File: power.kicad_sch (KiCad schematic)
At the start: 29 parts, among them Q1 DMPH4029LFGQ, Q2 BSS138-7-F, Q3 BSS138-7-F, U1 TPS56C230

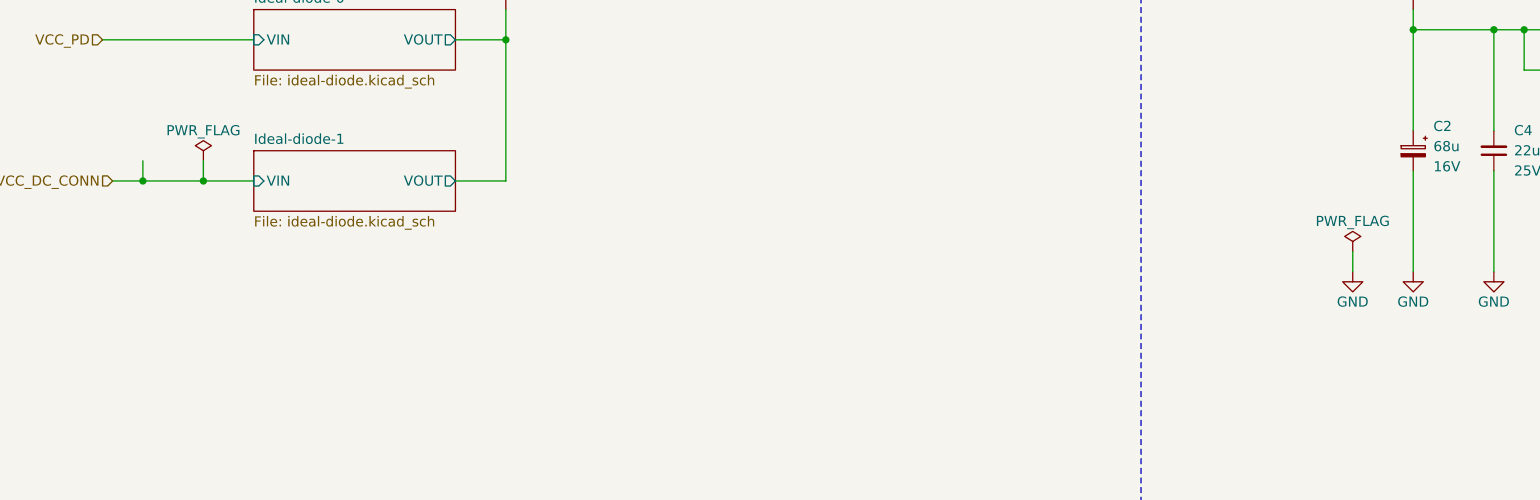
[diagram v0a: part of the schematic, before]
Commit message: [#79262] Add TVS to 12V power pins
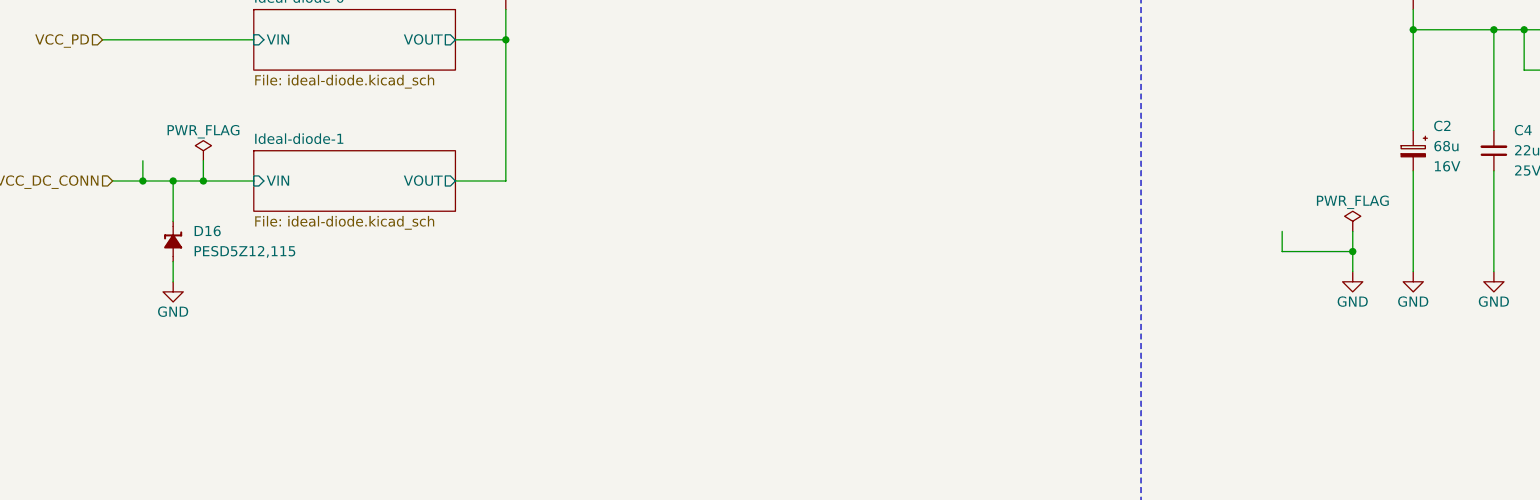
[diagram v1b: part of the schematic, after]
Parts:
- added D16: PESD5Z12, antmicro-footprints:SOD-523, symbol antmicroTVSDiodes:PESD5Z12
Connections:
- net GND: now also D16.2 (A)
- net VCC_DC_CONN: now also D16.1 (C)

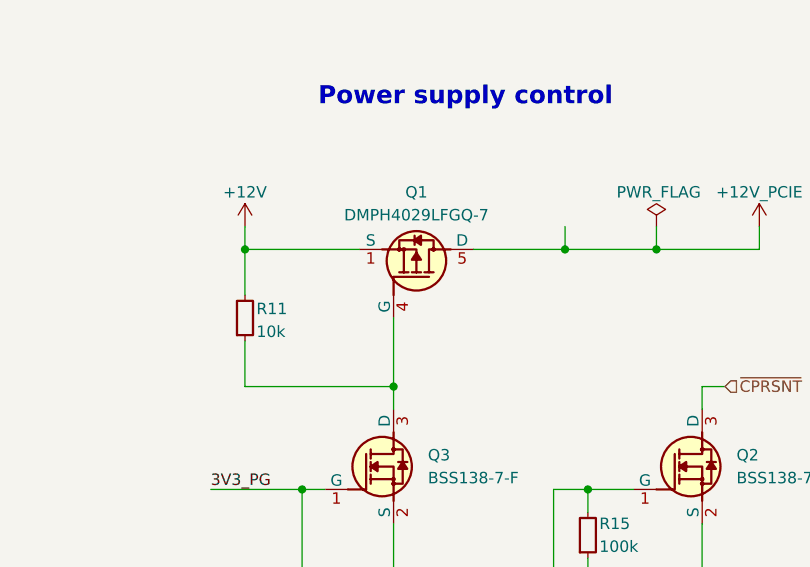
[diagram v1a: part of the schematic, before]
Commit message: [#79262] Further BOM consolidation
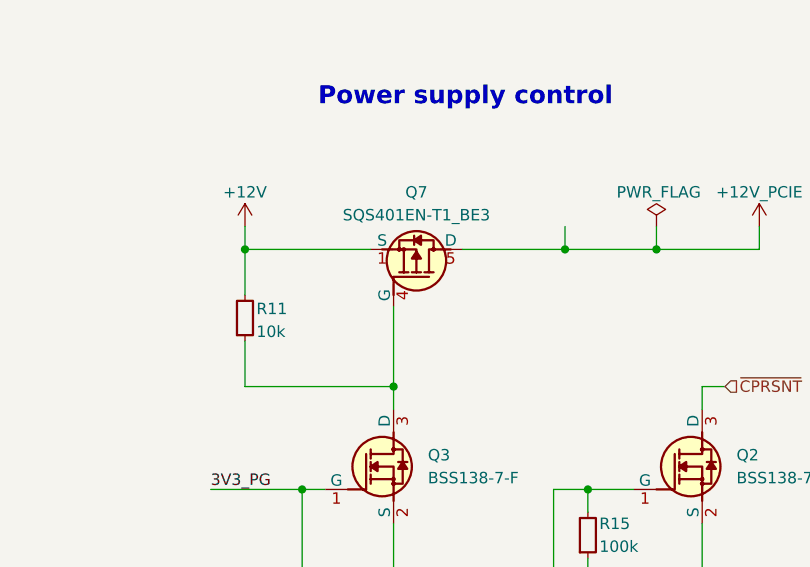
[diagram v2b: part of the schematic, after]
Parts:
- removed Q1: DMPH4029LFGQ, antmicro-footprints:PowerDI3333-8, symbol antmicroTransistorsFETsMOSFETsSingle:DMPH4029LFGQ
- added Q7: SQS401EN-T1_BE3, antmicro-footprints:Vishay_PowerPAK_1212-8_Single, symbol antmicroTransistorsFETsMOSFETsSingle:SQS401EN-T1_BE3
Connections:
- net +12V: now also Q7.1 (S), Q7.2 (S), Q7.3 (S)
- net +12V_PCIE: now also Q7.5 (D)
- net at Q3.3 (D), R11.1: now also Q7.4 (G)
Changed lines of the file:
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@@
 	(wire
 		(pts
-			(xy 99.06 203.2) (xy 99.06 210.82)
-		)
-		(stroke
-			(width 0)
-			(type default)
-		)
-	)
-	(wire
-		(pts
 			(xy 317.5 207.01) (xy 322.58 207.01)
 		)
@@
 	(wire
 		(pts
-			(xy 350.52 77.47) (xy 361.95 77.47)
+			(xy 99.06 201.93) (xy 99.06 210.82)
 		)
 		(stroke
@@
 	(wire
 		(pts
-			(xy 128.27 195.58) (xy 139.7 195.58)
+			(xy 350.52 77.47) (xy 361.95 77.47)
 		)
 		(stroke
@@
 	(wire
 		(pts
-			(xy 107.95 195.58) (xy 118.11 195.58)
+			(xy 128.27 195.58) (xy 139.7 195.58)
 		)
 		(stroke
@@
 	(wire
 		(pts
+			(xy 106.68 195.58) (xy 118.11 195.58)
+		)
+		(stroke
+			(width 0)
+			(type default)
+		)
+	)
+	(wire
+		(pts
 			(xy 361.95 102.87) (xy 361.95 93.98)
 		)
@@
 	(wire
 		(pts
-			(xy 82.55 195.58) (xy 95.25 195.58)
+			(xy 82.55 195.58) (xy 96.52 195.58)
 		)
 		(stroke
@@
 	)
 	(symbol
+		(lib_id "antmicroTransistorsFETsMOSFETsSingle:SQS401EN-T1_BE3")
+		(at 99.06 201.93 270)
+		(mirror x)
+		(unit 1)
+		(exclude_from_sim no)
+		(in_bom yes)
+		(on_board yes)
+		(dnp no)
+		(fields_autoplaced yes)
+		(property "Reference" "Q7"
+			(at 101.6 189.23 90)
+			(effects
+				(font
+					(size 1.27 1.27)
+					(thickness 0.15)
+				)
+			)
+		)
+		(property "Value" "SQS401EN-T1_BE3"
+			(at 88.9 186.69 0)
+			(effects
+				(font
+					(size 1.27 1.27)
+					(thickness 0.15)
+				)
+				(justify left bottom)
+				(hide yes)
+			)
+		)
+		(property "Footprint" "antmicro-footprints:Vishay_PowerPAK_1212-8_Single"
+			(at 86.36 186.69 0)
+			(effects
+				(font
+					(size 1.27 1.27)
+					(thickness 0.15)
+				)
+				(justify left bottom)
+				(hide yes)
+			)
+		)
+		(property "Datasheet" "https://www.vishay.com/docs/65529/sqs401en.pdf"
+			(at 83.82 186.69 0)
+			(effects
+				(font
+					(size 1.27 1.27)
+					(thickness 0.15)
+				)
+				(justify left bottom)
+				(hide yes)
+			)
+		)
+		(property "Description" "MOSFET, P Channel, 40 V, 16A, 0.047 ohm, PowerPAK 1212-8, Surface Mount"
+			(at 99.06 201.93 0)
+			(effects
+				(font
+					(size 1.27 1.27)
+				)
+				(hide yes)
+			)
+		)
+		(property "MPN" "SQS401EN-T1_BE3"
+			(at 101.6 191.77 90)
+			(effects
+				(font
+					(size 1.27 1.27)
+					(thickness 0.15)
+				)
+			)
+		)
+		(property "Manufacturer" "Vishay"
+			(at 81.28 186.69 0)
+			(effects
+				(font
+					(size 1.27 1.27)
+					(thickness 0.15)
+				)
+				(justify left bottom)
+				(hide yes)
+			)
+		)
+		(property "Author" "Antmicro"
+			(at 78.74 186.69 0)
+			(effects
+				(font
+					(size 1.27 1.27)
+					(thickness 0.15)
+				)
+				(justify left bottom)
+				(hide yes)
+			)
+		)
+		(property "License" "Apache-2.0"
+			(at 76.2 186.69 0)
+			(effects
+				(font
+					(size 1.27 1.27)
+					(thickness 0.15)
+				)
+				(justify left bottom)
+				(hide yes)
+			)
+		)
+		(pin "4"
+		)
+		(pin "1"
+		)
+		(pin "3"
+		)
+		(pin "5"
+		)
+		(pin "2"
+		)
+		(instances
+			(project "oculink-to-pcie-adapter"
+				(path "/44c3be85-0a18-4d93-a9a5-650ee09b6032/38f25804-42b6-4fac-b87c-d8c0064ff23c"
+					(reference "Q7")
+					(unit 1)
+				)
+			)
+		)
+	)
+	(symbol
 		(lib_id "antmicroTestPoints:TP_0.75mm_SMD")
 		(at 322.58 204.47 0)
@@
 					(unit 1)
 				)
-			)
-		)
-	)
-	(symbol
-		(lib_id "antmicroTransistorsFETsMOSFETsSingle:DMPH4029LFGQ")
-		(at 99.06 203.2 270)
-		(mirror x)
-		(unit 1)
-		(exclude_from_sim no)
-		(in_bom yes)
-		(on_board yes)
-		(dnp no)
-		(property "Reference" "Q1"
-			(at 101.6 189.23 90)
-			(effects
-				(font
-					(size 1.27 1.27)
-					(thickness 0.15)
-				)
-			)
-		)
-		(property "Value" "DMPH4029LFGQ"
-			(at 88.9 189.23 0)
-			(effects
-				(font
-					(size 1.27 1.27)
-					(thickness 0.15)
-				)
-				(justify left bottom)
-				(hide yes)
-			)
-		)
-		(property "Footprint" "antmicro-footprints:PowerDI3333-8"
-			(at 93.98 189.23 0)
-			(effects
-				(font
-					(size 1.27 1.27)
-					(thickness 0.15)
-				)
-				(justify left bottom)
-				(hide yes)
-			)
-		)
-		(property "Datasheet" "https://www.diodes.com/assets/Datasheets/DMPH4029LFGQ.pdf"
-			(at 91.44 189.23 0)
-			(effects
-				(font
-					(size 1.27 1.27)
-					(thickness 0.15)
-				)
-				(justify left bottom)
-				(hide yes)
-			)
-		)
-		(property "Description" "Power MOSFET, P Channel, 40 V, 22 A, 0.018 ohm, PowerDI 3333, Surface Mount"
-			(at 79.756 149.352 0)
-			(effects
-				(font
-					(size 1.27 1.27)
-				)
-				(hide yes)
-			)
-		)
-		(property "MPN" "DMPH4029LFGQ-7"
-			(at 101.6 191.77 90)
-			(effects
-				(font
-					(size 1.27 1.27)
-					(thickness 0.15)
-				)
-			)
-		)
-		(property "Manufacturer" "Diodes Incorporated"
-			(at 86.36 189.23 0)
-			(effects
-				(font
-					(size 1.27 1.27)
-					(thickness 0.15)
-				)
-				(justify left bottom)
-				(hide yes)
-			)
-		)
-		(property "Author" "Antmicro"
-			(at 83.82 189.23 0)
-			(effects
-				(font
-					(size 1.27 1.27)
-					(thickness 0.15)
-				)
-				(justify left bottom)
-				(hide yes)
-			)
-		)
-		(property "License" "Apache-2.0"
-			(at 81.28 189.23 0)
-			(effects
-				(font
-					(size 1.27 1.27)
-					(thickness 0.15)
-				)
-				(justify left bottom)
-				(hide yes)
-			)
-		)
-		(pin "2"
-		)
-		(pin "4"
-		)
-		(pin "5"
-		)
-		(pin "3"
-		)
-		(pin "1"
-		)
-		(instances
-			(project ""
-				(path "/44c3be85-0a18-4d93-a9a5-650ee09b6032/38f25804-42b6-4fac-b87c-d8c0064ff23c"
-					(reference "Q1")
-					(unit 1)
-				)

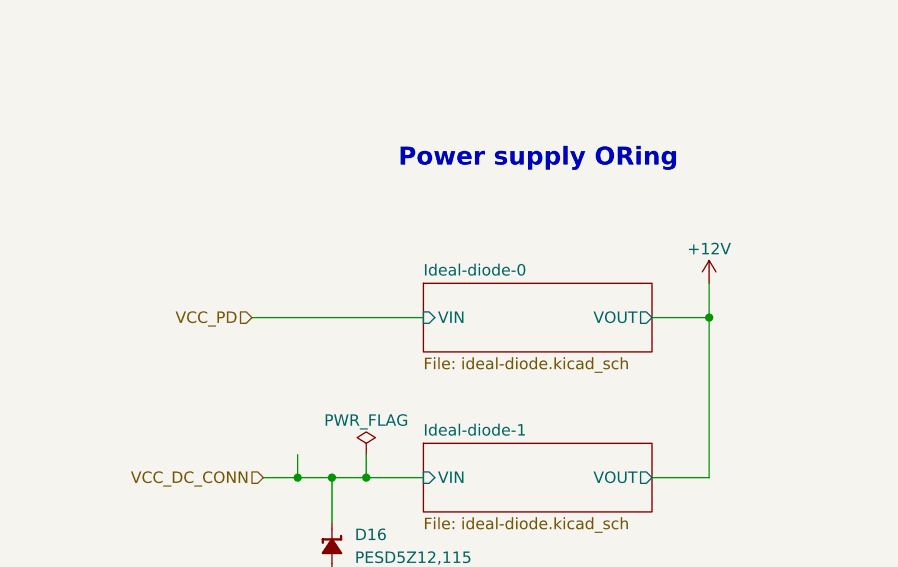
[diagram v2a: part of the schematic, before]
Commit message: [#79262] Reduce Q4 max Vgs
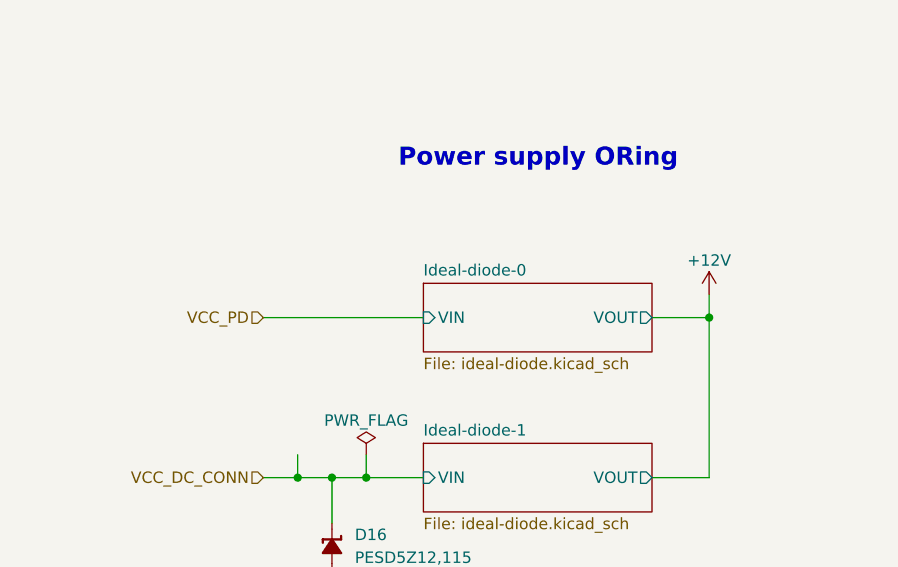
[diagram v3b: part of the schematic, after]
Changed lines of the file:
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@@
 	(wire
 		(pts
-			(xy 67.31 73.66) (xy 86.36 73.66)
+			(xy 68.58 73.66) (xy 86.36 73.66)
 		)
 		(stroke
@@
 	(wire
 		(pts
-			(xy 118.11 69.85) (xy 118.11 73.66)
+			(xy 118.11 71.12) (xy 118.11 73.66)
 		)
 		(stroke
@@
 	(hierarchical_label "VCC_PD"
 		(shape input)
-		(at 67.31 73.66 180)
+		(at 68.58 73.66 180)
 		(effects
 			(font
@@
 	(symbol
 		(lib_id "antmicropower:+12V_AON")
-		(at 118.11 69.85 0)
+		(at 118.11 71.12 0)
 		(unit 1)
 		(exclude_from_sim no)
@@
 		(dnp no)
 		(property "Reference" "#PWR085"
-			(at 118.11 73.66 0)
+			(at 118.11 74.93 0)
 			(effects
 				(font
@@
 		)
 		(property "Value" "+12V"
-			(at 118.11 66.04 0)
+			(at 118.11 67.31 0)
 			(effects
 				(font
@@
 		)
 		(property "Footprint" ""
-			(at 118.11 69.85 0)
+			(at 118.11 71.12 0)
 			(effects
 				(font
@@
 		)
 		(property "Datasheet" ""
-			(at 118.11 69.85 0)
+			(at 118.11 71.12 0)
 			(effects
 				(font
@@
 		)
 		(property "Description" ""
-			(at 118.11 69.85 0)
-			(effects
-				(font
+			(at 118.11 71.12 0)
+			(effects
+				(font
